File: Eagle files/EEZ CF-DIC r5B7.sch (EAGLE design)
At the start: 275 parts, among them IC1 VIPer35L, IC2 SI8233BB-D-IS1, IC3 LM5041B, IC4 LM258D, IC5 IR11688STRPBF, IC6 LM258D, IC7 TL103W, P1 T910W-50K, Q1 MMBT5551, Q10 BC856C, Q2 C3M0280090D, Q3 C3M0280090D, Q4 NYC0102BLT1G, Q5 IPW60R120P7, Q6 IPW60R120P7, Q7 FDD86250-F085, Q8 FDD86250-F085, Q9 BC856C, X1 39-30-3035, X2 22-05-7095, X3 B2B-ZR, X4 39-30-1020

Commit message: #4, #5, #6
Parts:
- removed D27: 1N5819HW-7-F, diode:DIODE-SOD323-W
- removed D28: BAS316, EEZ_Lib1:DIODESOD323R
- removed SH4: (no value), EEZ_Lib1:SHORTNOHOLE
- added C81: N.C., rcl:C-EUC0805
- added JP10: JP2-NOCUT, EEZ_Lib1:JP2-NOCUT
- added R100: 180K, rcl:R-EU_R0805
- added R101, R103: 39K, rcl:R-EU_R0805
- added R102: 18K, rcl:R-EU_R0805
- added R99: 10K, rcl:R-EU_R0805
- C14: value 1n/1kV -> 2n2/1kV
- C23: value 1500u -> 470u; device EEZ_Lib1:ECAP5G_13MM -> EEZ_Lib1:ECAP5G_10.5MM
- C27: value 100p -> 47p
- C41, C63, C70: value 4n7/200V -> 4n7/500V
- C43: value 10n -> 100n
- C57: device EEZ_Lib1:ECAPH35.5-2A -> EEZ_Lib1:ECAPH35.5A
- C58: value N.C. -> 1u/100V; device EEZ_Lib1:ECAP7.5G_18MM -> rcl:C-EUC1206
- C59: value 1u/100V -> 47p/200V; device rcl:C-EUC1206 -> rcl:C-EUC0805
- C71: value 100n -> 47p/200V; device rcl:C-EUC0603 -> rcl:C-EUC0805
- C72: value 1n -> 100n; device rcl:C-EUC0805 -> rcl:C-EUC0603
- C73: value 100n -> 1n; device rcl:C-EUC0603 -> rcl:C-EUC0805
- C74: value 47p -> 100n; device rcl:C-EUC0805 -> rcl:C-EUC0603
- C75: value 100n -> 47p; device rcl:C-EUC0603 -> rcl:C-EUC0805
- C76: value 100p -> 100n; device rcl:C-EUC0805 -> rcl:C-EUC0603
- C77: value 470p -> 100p
- C78: value N.C. -> 470p; device EEZ_Lib1:ECAP1206 -> rcl:C-EUC0805
- C79: value 1u -> N.C.; device rcl:C-EUC0805 -> EEZ_Lib1:ECAP1206
- C80: value N.C. -> 1u
- D26: value 1N5819HW-7-F -> BAS316; device diode:DIODE-SOD323-W -> EEZ_Lib1:DIODESOD323R
- D7: value 1N5819HW-7-F -> SS115; device diode:DIODE-SOD323-W -> EEZ_Lib1:SCHOTTKYSMA_DO-214AC
- JP3: value 0R-JUMPA -> JP2-NOCUT; device jump-0r-smd:0R-JUMPA -> EEZ_Lib1:JP2-NOCUT
- JP4: value JP2-NOCUT -> 0R-JUMPA; device EEZ_Lib1:JP2-NOCUT -> jump-0r-smd:0R-JUMPA
- JP6, JP9: value JP2-NOCUT -> JP3-CUT; device EEZ_Lib1:JP2-NOCUT -> EEZ_Lib1:JP3-CUT
- JP8: value JP3-CUT -> JP2-NOCUT; device EEZ_Lib1:JP3-CUT -> EEZ_Lib1:JP2-NOCUT
- R11: value 120R -> 36K; device rcl:R-EU_R0805 -> rcl:R-EU_R1206
- R12: value 100K -> 120R; device rcl:R-EU_R1206 -> rcl:R-EU_R0805
- R14: value 120R -> 100K; device rcl:R-EU_R0805 -> rcl:R-EU_R1206
- R15: value N.C. -> 120R
- R16, R38: value 47K -> N.C.
- R17: value 1K -> 16K
- R18: value 12K -> 1K
- R19: value 1K8 -> 4K7
- R20: value 47K -> 1K8
- R21: value 1K -> 47K
- R22: value 100K -> 1K; device rcl:R-EU_R1206 -> rcl:R-EU_R0805
- R23: value 10R -> 100K; device rcl:R-EU_R0805 -> rcl:R-EU_R1206
- R24: value 10K -> 10R
- R25: value 33R -> 10K
- R27: value 100K -> N.C.; device rcl:R-EU_R1206 -> rcl:R-EU_R0805
- R28: value 100R -> 100K; device rcl:R-EU_R0805 -> rcl:R-EU_R1206
- R30: value 22R/2-3W -> 100R; device rcl:R-EU_R2512 -> rcl:R-EU_R0805
- R31: value 100K -> 22R/2-3W; device rcl:R-EU_R1206 -> rcl:R-EU_R2512
- R32: value 22R/2-3W -> 86K6; device rcl:R-EU_R2512 -> rcl:R-EU_R1206
- R33: value 30K -> 22R/2-3W; device rcl:R-EU_R0805 -> rcl:R-EU_R2512
- R34: value 1R -> 30K
- R35: value 33R -> 1R
- R39: value 1R -> 47K
- R40: value 22R/2-3W -> 1R; device rcl:R-EU_R2512 -> rcl:R-EU_R0805
- R41: value 1K -> 22R/2-3W; device rcl:R-EU_R0805 -> rcl:R-EU_R2512
- R42: value 22R/2-3W -> 1K; device rcl:R-EU_R2512 -> rcl:R-EU_R0805
- R43, R72: value 10R -> N.C.; device rcl:R-EU_R0805 -> rcl:R-EU_R2512
- R44, R54: value 1K -> 10R
- R45: value 10R -> 1K
- R46: value 7K5 -> 10R
- R47: value 86K6 -> 8K2
- R49: value 10R -> 86K6
- R50: value 15K -> 10R
- R51: value 4K7 -> 15K
- R52: value 86K6 -> 4K7
- R53: value 10R -> 56K
- R55: value 6R2 -> 1K
- R56: value 1K -> 6R2
- R58: value 4K7 -> 1K
- R59: value 5K6 -> 4K7
- R6, R7: value N.C. -> 4K7
- R60: value 30K -> 5K6
- R61: value 1K -> 30K
- R62: value 30K -> 1K
- R63: value 10K -> 30K
- R64: value 1K -> 10K
- R66: value 120R -> 1K
- R67: value N.C. -> 120R; device rcl:R-EU_R1210 -> rcl:R-EU_R0805
- R69: value 22R/2-3W -> N.C.
- R70: value 3R3 -> N.C.; device rcl:R-EU_R0805 -> rcl:R-EU_R1210
- R71: value N.C. -> 1K; device rcl:R-EU_R2512 -> rcl:R-EU_R0805
- R73: value 47K -> 10R
- R74: value 3R3 -> 10R
- R75: value 22R/2-3W -> 100K; device rcl:R-EU_R2512 -> rcl:R-EU_R0805
- R76: value 22R/2-3W -> 10R; device rcl:R-EU_R2512 -> rcl:R-EU_R0805
- R77: value 10K -> 1K
- R78: value 470R -> 22R/2-3W; device rcl:R-EU_R0805 -> rcl:R-EU_R2512
- R79: value 470R -> N.C.; device rcl:R-EU_R0805 -> rcl:R-EU_R2512
- R8: value 100K -> 36K
- R80: value 150K -> 10K
- R81: value 10K -> 470R
- R82: value 1K -> 470R
- R83: value 30K -> 150K
- R84: value 1K8 -> 10K
- R86: value 86K6 -> 30K
- R88: value 3K3 -> 1K
- R89: value 1K -> 86K6
- R9: value 220K -> 100K
- R90: value 5K6 -> 1K8
- R91: value 7K5 -> 3K3
- R92: value 220R -> 1K
- R93: value 10K -> 5K6
- R94: value 10K -> 7K5
- R95: value 150K -> 220R
- R96: value 39K -> N.C.
- R97: value 15K -> N.C.
- R98: value 47K -> 10K
- TP5: device EEZ_connectors:TEST-PIN1.2 -> EEZ_connectors:TEST_POINT-2
- TP6: device EEZ_connectors:TEST_POINT-2 -> EEZ_Lib1:JUMPER-2PIN-2MM
- ZD1: value BZX384-C15 -> BZX384-C13
- ZD4: value MMSZ5V1T1G -> BZT52C6V2; device EEZ_Lib1:ZENER-DIODESOD323 -> EEZ_Lib1:ZENER-DIODESOD123
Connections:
- removed net +14V: C29.2, C30.2, C52.1, C53.1, IC4P.V+, JP1.2, OK2.A, R23.2, R36.2, R45.2
- removed net N$67 (its old number): C70.1, R75.2, R76.2
- removed net N$74: D26.C, IC5.GATE1, R70.2
- removed net N$75: D27.C, IC5.GATE2, R74.2
- removed net S1_OUT: SH3.GND_A, TR3.S1
- removed net S2_DOT_OUT: SH4.GND_B, TR3.S2_DOT
- removed net SR_OUT1: D26.A, Q7.G, R70.1
- removed net SR_OUT2: D27.A, Q8.G, R74.1
- new net +12V: C29.2, C30.2, C52.1, C53.1, IC4P.V+, JP1.2, OK2.A, R24.2, R37.2, R46.2
- new net G1_OUT: Q7.G, R73.1
- new net G2_OUT: Q8.G, R76.1
- new net GATE1: IC5.GATE1, R73.2
- new net GATE2: IC5.GATE2, R76.2
- new net N$66: C70.1, R78.2, R79.2
- new net N$71: C73.1, JP6.COM
- new net N$73: R96.1, R97.2
- new net N$77: R97.1, TP6.1
- new net N$78: R11.2, R8.2
- new net S_COMM: JP6.NC, SH3.GND_A, TR3.S1, TR3.S2_DOT
- new net VD1: C59.2, IC5.VD1, R71.1
- new net VD2: C71.2, IC5.VD2, R77.2
- net !FAULT: now also D26.C; no longer D28.C
- net +2.5VREF: now also C80.1, R84.2, R90.1; no longer C79.1, R81.2, R87.1
- net +5VREF: now also R100.1, R44.1, R60.2, R98.1; no longer R43.1, R58.2, R93.1, R95.1
- net +6V_REC: now also R15.1, R18.1; no longer R14.1, R17.1
- net -7V_REC: now also R12.1; no longer R11.1
- net 0V: now also R19.1, R21.2, R40.1, R40.2; no longer R18.1, R19.2, R38.2, R39.1, TP5.P$1
- net 12V_COMM: now also JP4-0R.2; no longer JP3-0R.2
- net AGND: now also R102.2, R35.1, R35.2, R47.2, R51.2, R53.2, R58.2, R66.2, R99.2; no longer R33.1, R34.2, R46.2, R50.2, R52.2, R56.2, R61.2, R94.2, R97.2
- net AUX_AC: now also R16.2; no longer R15.2
- net CLAMP_C: now also R41.1, R43.1, R49.2; no longer R40.1, R42.1, R48.2
- net COMP: now also JP10.1; no longer JP9.1
- net CT_OUT+: now also R25.1; no longer R24.1
- net CT_OUT-: now also R25.2, R56.2, R58.1; no longer R24.2, R55.2, R57.1
- net DC_BUS: now also JP3.1, R23.1; no longer JP4.1, R22.1
- net FB: now also R48.1, R57.1, R61.1; no longer R47.1, R56.1, R60.1
- net FB2: now also R22.1; no longer R21.1
- net GND: now also C58.2, C59.1, C71.1, C72.2, C74.2, C76.2, C79.-, C81.2, JP4-0R.3, R72.1, R75.2, TP5.GND, TP6.2; no longer C58.-, C59.2, C71.2, C73.2, C75.2, C78.-, C79.2, JP3-0R.3, R71.1, R73.2, TP6.GND
- net HD: now also R29.2; no longer R28.2
- net HI_OUT: now also R27.2; no longer R25.2
- net LD: now also R30.2; no longer R29.2
- net LO_OUT: now also R36.1, R38.1; no longer R35.1, R37.1
- net L_PUSH: now also R31.2; no longer R30.2
- net N$1: now also D26.A; no longer D28.A
- net N$10: now also C75.2, R89.1, R93.1; no longer C74.2, R86.1, R90.1
- net N$100: now also R52.1; no longer R51.1
- net N$11: now also R82.2; no longer R79.2
- net N$12: now also R83.1, R87.2; no longer R80.1, R84.2
- net N$13: now also R50.1; no longer R49.1
- net N$130: now also R42.2; no longer R41.2
- net N$132: now also R80.2, R84.1; no longer R77.2, R81.1
- net N$134: now also C77.1, R95.2; no longer C76.1, R92.2
- net N$135: now also R18.2; no longer R17.2
- net N$137: now also R11.1; no longer R9.2
- net N$14: now also R54.1; no longer R53.1
- net N$141: now also R17.1, R19.2; no longer R15.1, R18.2
- net N$144: now also R12.2; no longer R11.2
- net N$146: now also R15.2; no longer R14.2
- net N$152: now also R21.1; no longer R20.1
- net N$155: now also R17.2; no longer R16.2
- net N$16: now also R81.2; no longer R78.2
- net N$17: now also R33.1; no longer R32.1
- net N$18: now also R75.1; no longer R73.1
- net N$19: now also R53.1; no longer R52.1
- net N$2: now also R28.2, R32.1; no longer R27.2, R31.1
- net N$20: now also R14.2, R20.1; no longer R13.2, R19.1
- net N$21: now also R26.1; no longer R25.1
- net N$22: now also R51.1; no longer R50.1
- net N$25: now also R45.1; no longer R44.1
- net N$26: now also R59.1, R63.1; no longer R58.1, R62.1
- net N$28: now also C73.2, R86.2; no longer C72.2, R83.2
- net N$29: now also R36.2, R39.1; no longer R35.2, R38.1
- net N$30: now also R48.2, R49.1; no longer R47.2, R48.1
- net N$31: now also R24.1; no longer R23.1
- net N$32: now also R42.1; no longer R41.1
- net N$34: now also R61.2; no longer R60.2
- net N$35: now also R41.2, R43.2; no longer R40.2, R42.2
- net N$36: now also R29.1; no longer R28.1
- net N$37: now also R55.2; no longer R54.2
- net N$39: now also C76.1, JP8.1; no longer C75.1, JP7.1
- net N$40: now also R30.1; no longer R29.1
- net N$42: now also R64.1; no longer R63.1
- net N$44: now also JP10.2; no longer JP9.2
- net N$45: now also R27.1; no longer R26.1
- net N$46: now also C72.1, C74.1, JP7.2, R74.1, R90.2, R91.2; no longer C71.1, C73.1, JP6.2, R72.1, R87.2, R88.2
- net N$48: now also R34.2; no longer R33.2
- net N$49: now also R13.2, R14.1; no longer R12.2, R13.1
- net N$5: now also R31.1, R33.2; no longer R30.1, R32.2
- net N$50: now also R86.1, R87.1, R93.2, R94.2, R96.2; no longer R83.1, R84.1, R90.2, R91.2
- net N$51: now also R52.2, R62.1; no longer R51.2, R61.1
- net N$52: now also R38.2; no longer R37.2
- net N$53: now also R80.1, R85.2; no longer R77.1, R82.2
- net N$54: now also R46.1; no longer R45.1
- net N$56: now also R56.1; no longer R54.1
- net N$57: now also C81.1, JP9.COM; no longer C80.1, JP8.COM
- net N$58: now also JP9.NO; no longer JP8.NO
- net N$59: now also R66.1; no longer R65.1
- net N$6: now also R23.2, R28.1; no longer R22.2, R27.1
- net N$60: now also R13.1, R9.2; no longer R12.1, R8.2
- net N$61: now also R99.1; no longer R94.1
- net N$62: now also R98.2; no longer R93.2
- net N$63: now also R37.1; no longer R36.1
- net N$64: now also C77.2, R85.1, R88.2, R92.1; no longer C76.2, R82.1, R85.2, R89.1
- net N$68: now also R101.2, R102.1, R103.1; no longer R96.2, R97.1, R98.1
- net N$7: now also R60.1, R65.1; no longer R59.1, R64.1
- net N$70: now also R100.2, R101.1; no longer R95.2, R96.1
- net N$76: now also C75.1, C78.1; no longer C74.1, C77.1
- net N$8: now also R70.1; no longer R67.1
- net N$9: now also C78.2, R89.2; no longer C77.2, R86.2
- net NFB_OFFSET: now also C79.+, R88.1, R94.1, R95.1; no longer C78.+, R85.1, R91.1, R92.1
- net OK_A: now also R91.1; no longer R88.1
- net POUT+: now also C58.1, R67.1; no longer C58.+, C59.1, R66.1, SH4.GND_A
- net PREG_OUT+: now also JP4-0R.1, JP6.NO, R70.2, R72.2, R83.2, TP5.TIP; no longer C72.1, JP3-0R.1, R66.2, R71.2, R80.2, TP6.TIP
- net PULL: now also R54.2; no longer R53.2
- net PUSH: now also R50.2; no longer R49.2
- net REF: now also R44.2; no longer R43.2
- net S1_DOT_OUT: now also Q8.D, R77.1, R78.1, R79.1; no longer IC5.VD1, Q7.D, R68.1, R69.1
- net S2_OUT: now also Q7.D, R68.1, R69.1, R71.2; no longer IC5.VD2, Q8.D, R75.1, R76.1
- net SYNC_VCC: now also R74.2; no longer R72.2
- net UVLO: now also R103.2, R32.2, R45.2, R47.1; no longer R31.2, R44.2, R46.1, R98.2
- net U_CTRL: now also JP9.NC; no longer JP8.NC
- net U_MON1: now also R92.2; no longer R89.2
- net V+: now also JP7.1, R22.2, R81.1, R82.1; no longer JP6.1, R21.2, R78.1, R79.1
- net V-: now also JP8.2; no longer JP7.2
- net VIPER+: now also JP3.2; no longer JP4.2
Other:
- note added: "100R"
- note added: "10K"
- note added: "150K"
- note added: "200K"
- note added: "2K2"
- note added: "2K7"
- note added: "Join GND traces to the IC5 VS input as shown on the schematic."
- note added: "Routing between the drain of the MOSFET and the IC5 pin must be particularly optimized"
- note removed: "8K2"
- note removed: "Routing between the drain of the MOSFET and the IC pin must be particularly optimized"
- moved on the sheet: C14, C57, C59, C60, C61, C62, C63, C64, C65, C66, C67, C68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

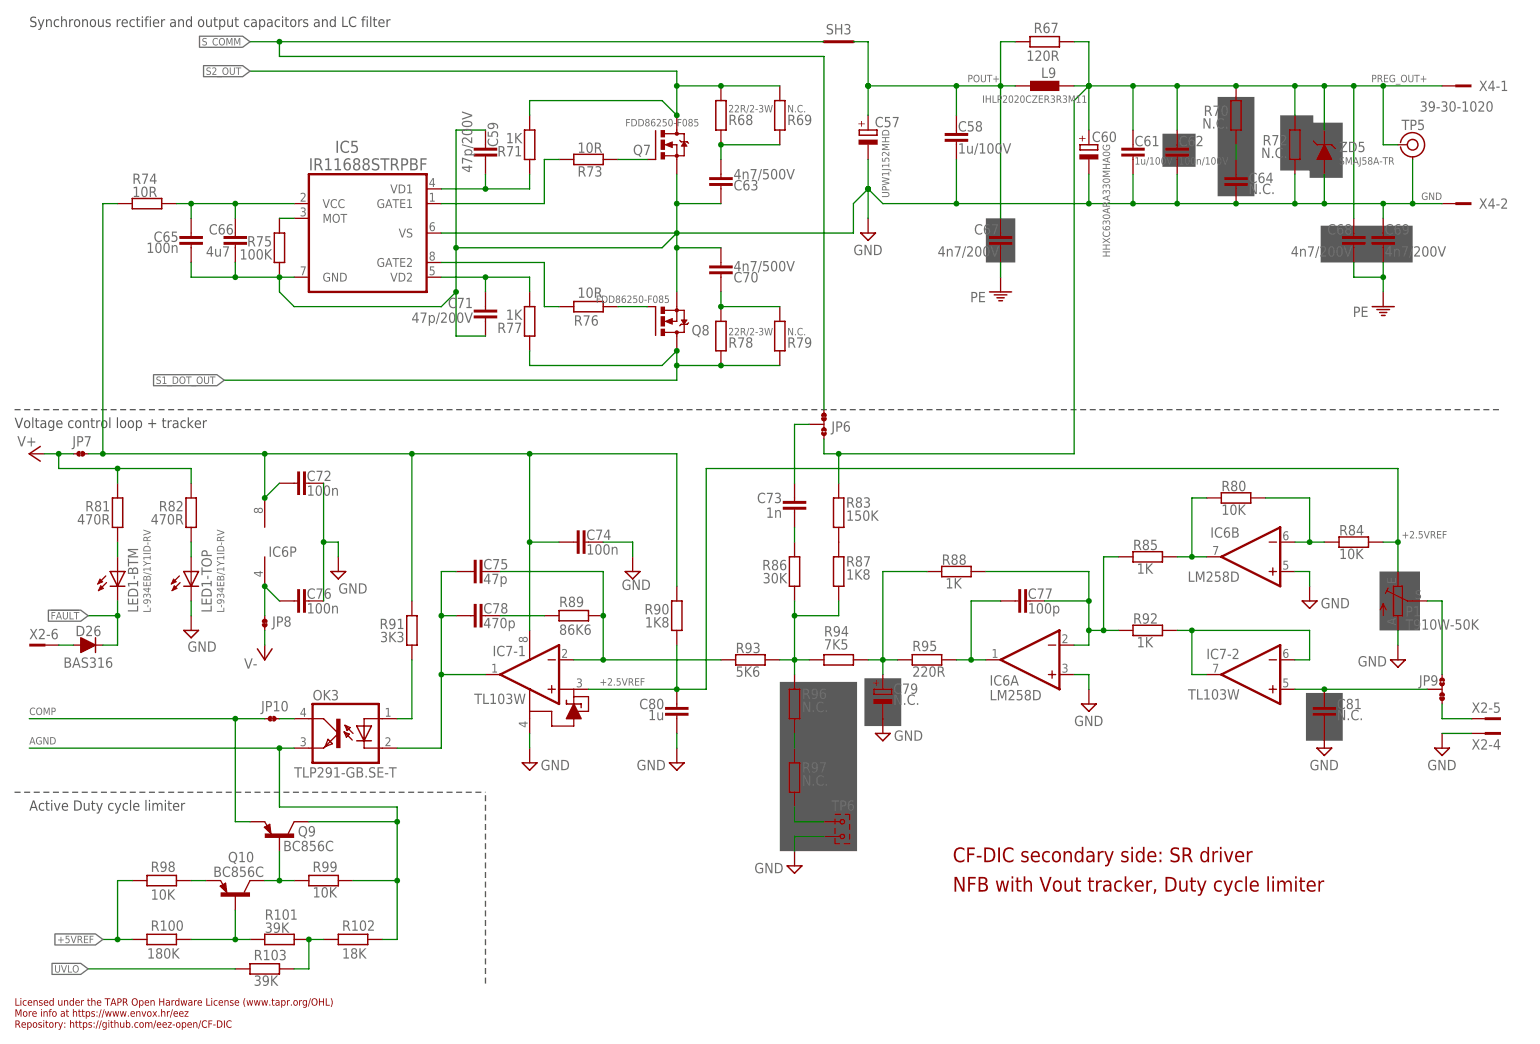
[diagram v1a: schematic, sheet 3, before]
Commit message: changed SR mosfets package
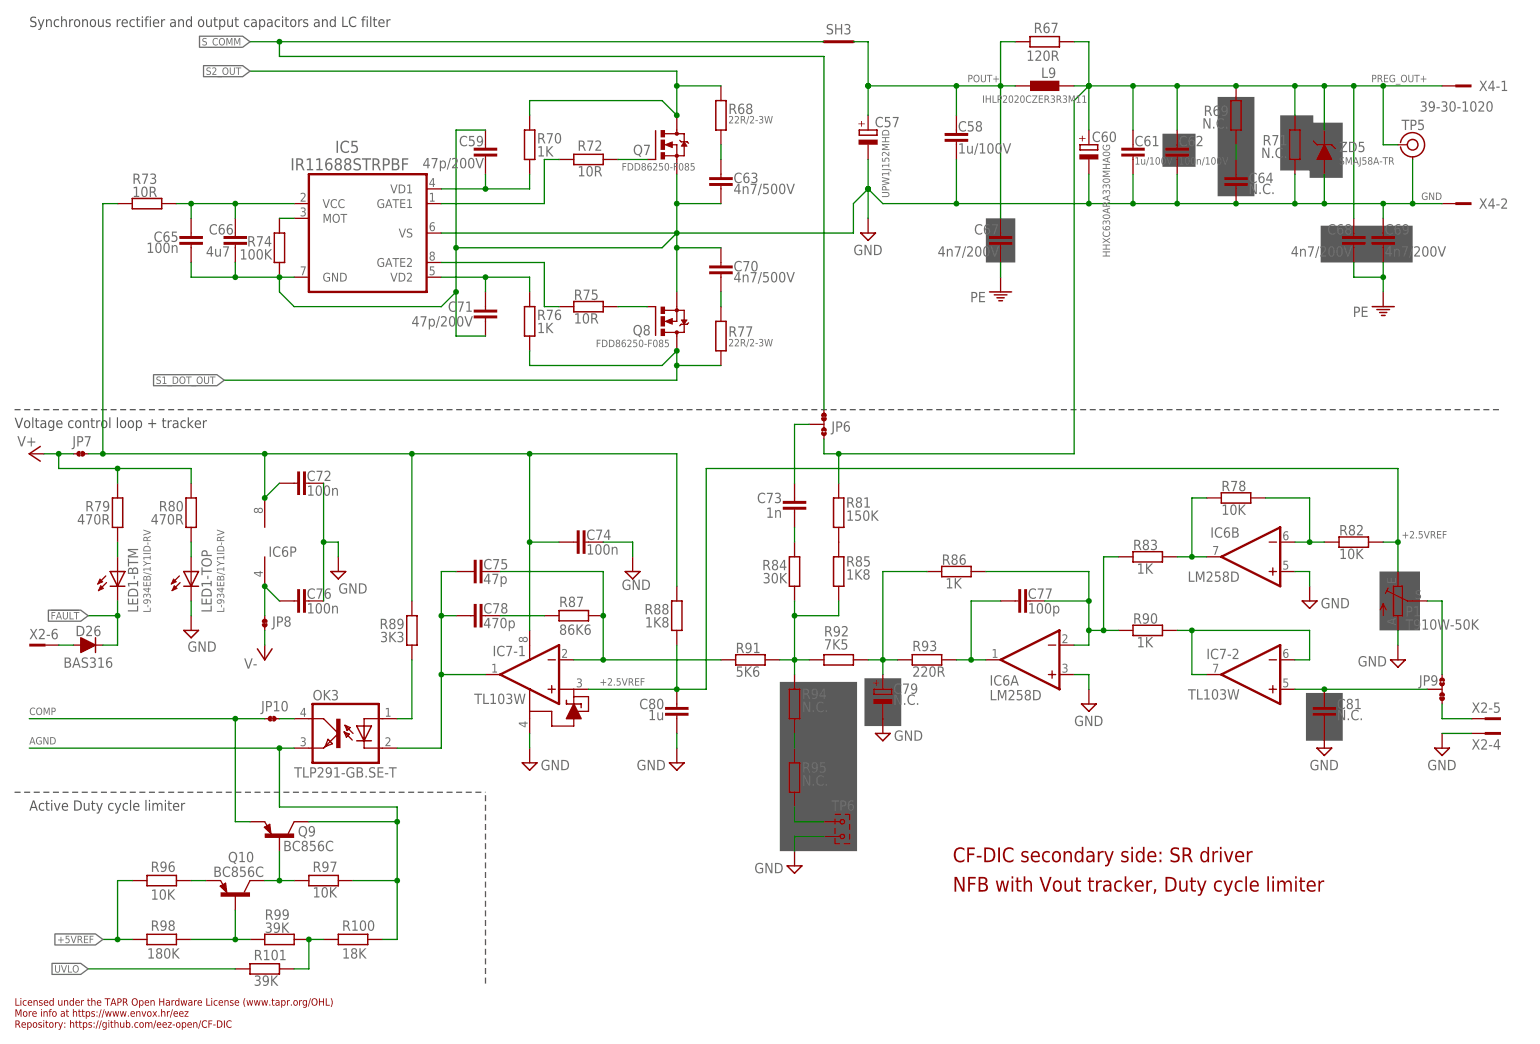
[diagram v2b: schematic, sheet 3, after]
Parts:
- removed R102: 18K, rcl:R-EU_R0805
- removed R103: 39K, rcl:R-EU_R0805
- D7: value SS115 -> SS100B
- Q7, Q8: device EEZ_Lib1:N-MOSFETTO263 -> EEZ_Lib1:N-MOSFETDPAK
- R100: value 180K -> 18K
- R61: value 30K -> 86K6
- R69: device rcl:R-EU_R2512 -> rcl:R-EU_R1210
- R70: value N.C. -> 1K; device rcl:R-EU_R1210 -> rcl:R-EU_R0805
- R71: value 1K -> N.C.; device rcl:R-EU_R0805 -> rcl:R-EU_R2512
- R72: value N.C. -> 10R; device rcl:R-EU_R2512 -> rcl:R-EU_R0805
- R74: value 10R -> 100K
- R75: value 100K -> 10R
- R76: value 10R -> 1K
- R77: value 1K -> 22R/2-3W; device rcl:R-EU_R0805 -> rcl:R-EU_R2512
- R78: value 22R/2-3W -> 10K; device rcl:R-EU_R2512 -> rcl:R-EU_R0805
- R79: value N.C. -> 470R; device rcl:R-EU_R2512 -> rcl:R-EU_R0805
- R80: value 10K -> 470R
- R81: value 470R -> 150K
- R82: value 470R -> 10K
- R83: value 150K -> 1K
- R84: value 10K -> 30K
- R85, R88: value 1K -> 1K8
- R86: value 30K -> 1K
- R87: value 1K8 -> 86K6
- R89: value 86K6 -> 3K3
- R90: value 1K8 -> 1K
- R91: value 3K3 -> 5K6
- R92: value 1K -> 7K5
- R93: value 5K6 -> 220R
- R94: value 7K5 -> N.C.
- R95: value 220R -> N.C.
- R96, R97: value N.C. -> 10K
- R98: value 10K -> 180K
- R99: value 10K -> 39K
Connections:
- net +2.5VREF: now also R82.2, R88.1; no longer R84.2, R90.1
- net +5VREF: now also R96.1; no longer R100.1
- net AGND: now also R100.2, R97.2; no longer R102.2, R99.2
- net G1_OUT: now also R72.1; no longer R73.1
- net G2_OUT: now also R75.1; no longer R76.1
- net GATE1: now also R72.2; no longer R73.2
- net GATE2: now also R75.2; no longer R76.2
- net GND: now also R71.1, R74.2; no longer R72.1, R75.2
- net N$10: now also R87.1, R91.1; no longer R89.1, R93.1
- net N$11: now also R80.2; no longer R82.2
- net N$12: now also R81.1, R85.2; no longer R83.1, R87.2
- net N$132: now also R78.2, R82.1; no longer R80.2, R84.1
- net N$134: now also R93.2; no longer R95.2
- net N$16: now also R79.2; no longer R81.2
- net N$18: now also R74.1; no longer R75.1
- net N$28: now also R84.2; no longer R86.2
- net N$46: now also R73.1, R88.2, R89.2; no longer R74.1, R90.2, R91.2
- net N$50: now also R84.1, R85.1, R91.2, R92.2; no longer R86.1, R87.1, R93.2, R96.2
- net N$53: now also R78.1, R83.2; no longer R80.1, R85.2
- net N$61: now also R97.1; no longer R99.1
- net N$62: now also R96.2; no longer R98.2
- net N$64: now also R83.1, R86.2, R90.1; no longer R85.1, R88.2, R92.1
- net N$66: now also R77.2; no longer R78.2, R79.2
- net N$67: no longer R69.2
- net N$68: now also R100.1, R101.1, R99.2; no longer R101.2, R102.1, R103.1
- net N$70: now also R98.2, R99.1; no longer R100.2, R101.1
- net N$73: now also R94.1, R95.2; no longer R96.1, R97.2
- net N$77: now also R95.1; no longer R97.1
- net N$8: now also R69.1; no longer R70.1
- net N$9: now also R87.2; no longer R89.2
- net NFB_OFFSET: now also R86.1, R92.1, R93.1; no longer R88.1, R94.1, R95.1
- net OK_A: now also R89.1; no longer R91.1
- net PREG_OUT+: now also R69.2, R71.2, R81.2; no longer R70.2, R72.2, R83.2
- net S1_DOT_OUT: now also R76.1; no longer R78.1, R79.1
- net S2_OUT: now also R70.2; no longer R69.1, R71.2
- net SYNC_VCC: now also R73.2; no longer R74.2
- net UVLO: now also R101.2; no longer R103.2
- net U_MON1: now also R90.2; no longer R92.2
- net V+: now also R79.1, R80.1; no longer R81.1, R82.1
- net VD1: now also R70.1; no longer R71.1
- net VD2: now also R76.2; no longer R77.2
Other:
- note removed: "47K"
- moved on the sheet: R100, R101, R69, R70, R71, R72, R73, R74, R75, R76, R77, R78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
